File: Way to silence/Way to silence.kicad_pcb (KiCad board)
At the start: 2 copper layers, 60 parts, among them J1 SD Card Connector, J2 Screw_Terminal_01x02, J3 5V_Terminal, J4 Battery_Terminal, Q1 BC817, Q2 BC817, SW1 SW_SPDT, U1 ESP32-WROOM-32-N16, U2 SM5308, U3 CP2102-GMR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

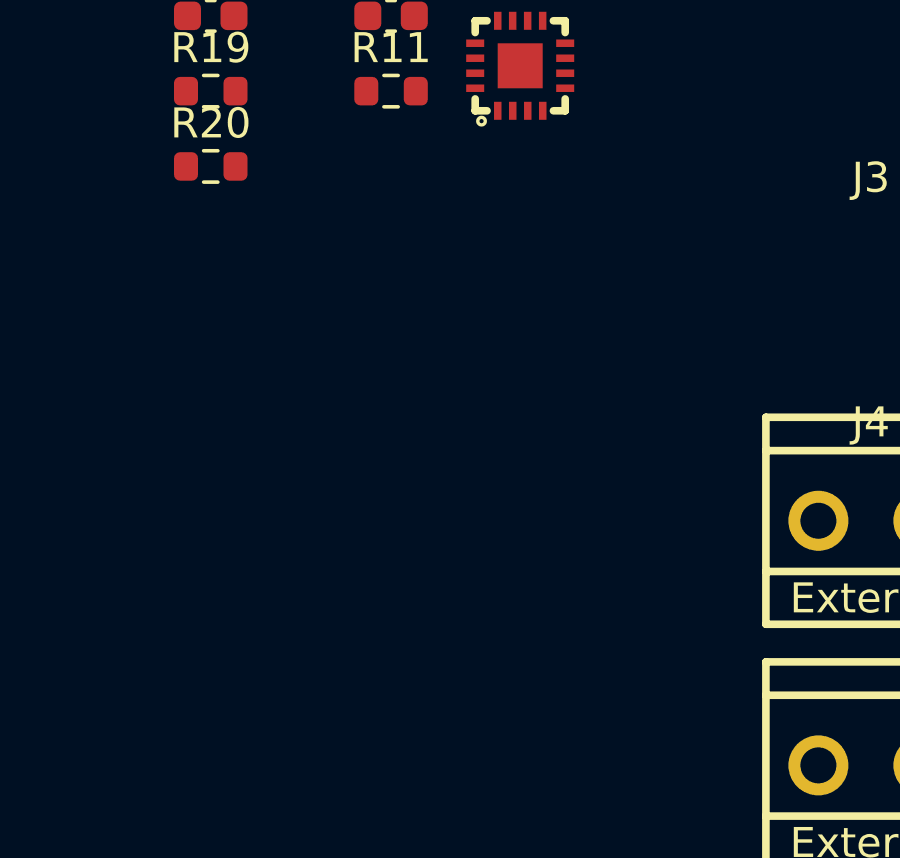
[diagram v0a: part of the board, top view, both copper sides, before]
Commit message: [ADD] Missing footprints
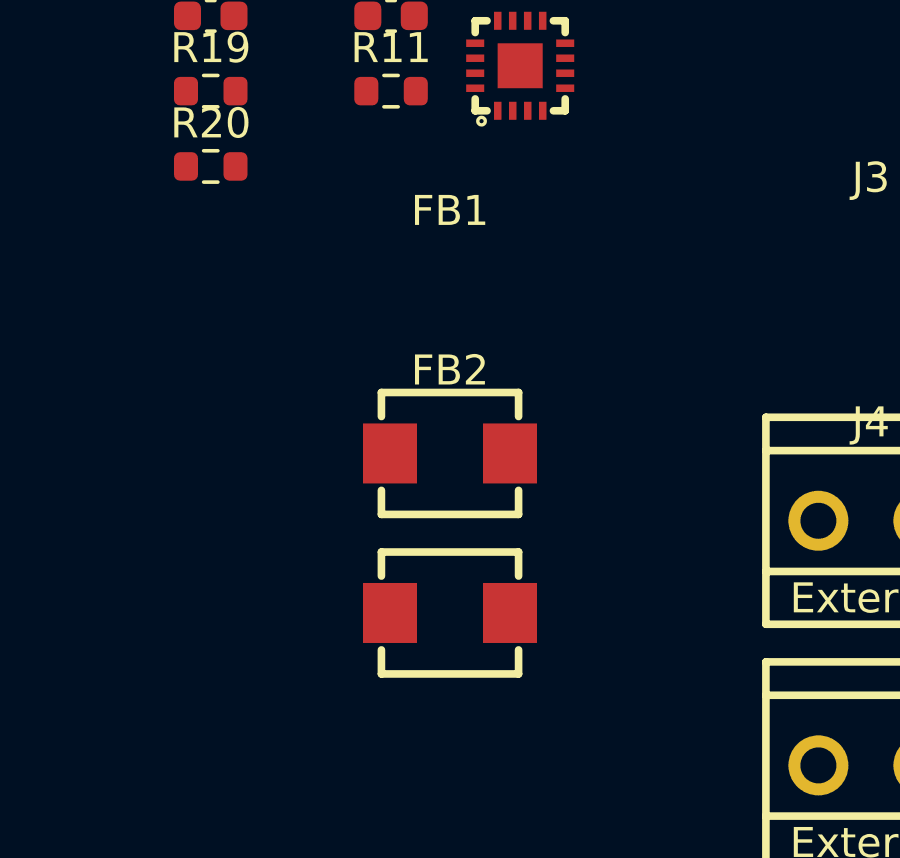
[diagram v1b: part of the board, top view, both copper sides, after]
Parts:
- added FB1: FerriteBead, Way to silence:Inductor, F.Cu at (111.2, 55.6)
- added FB2: FerriteBead, Way to silence:Inductor, F.Cu at (111.2, 61.0)
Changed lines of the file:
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@@
     )
   )
+  (footprint "Way to silence:Inductor" (layer "F.Cu")
+    (at 111.22 55.642)
+    (property "LCSC" "C2847468")
+    (property "Sheetfile" "I2SAmp.kicad_sch")
+    (property "Sheetname" "I2S Amp")
+    (property "ki_description" "Ferrite bead")
+    (property "ki_keywords" "L ferrite bead inductor filter")
+    (attr smd)
+    (fp_text reference "FB1" (at 0 -8.08 unlocked) (layer "F.SilkS")
+        (effects (font (size 1 1) (thickness 0.1)))
+    )
+    (fp_text value "FerriteBead" (at 0 -6.58 unlocked) (layer "F.Fab")
+        (effects (font (size 1 1) (thickness 0.15)))
+    )
+    (fp_text user "${REFERENCE}" (at 0 -5.08 unlocked) (layer "F.Fab")
+        (effects (font (size 1 1) (thickness 0.15)))
+    )
+    (fp_line (start -2.286 -2.032) (end 2.286 -2.032)
+      (stroke (width 0.254) (type solid)) (layer "F.SilkS"))
+    (fp_line (start -2.286 -1.231) (end -2.286 -2.032)
+      (stroke (width 0.254) (type solid)) (layer "F.SilkS"))
+    (fp_line (start -2.286 2.032) (end -2.286 1.231)
+      (stroke (width 0.254) (type solid)) (layer "F.SilkS"))
+    (fp_line (start 2.286 -2.032) (end 2.286 -1.231)
+      (stroke (width 0.254) (type solid)) (layer "F.SilkS"))
+    (fp_line (start 2.286 1.231) (end 2.286 2.032)
+      (stroke (width 0.254) (type solid)) (layer "F.SilkS"))
+    (fp_line (start 2.286 2.032) (end -2.286 2.032)
+      (stroke (width 0.254) (type solid)) (layer "F.SilkS"))
+    (pad "1" smd rect (at -2 0 90) (size 2 1.8) (layers "F.Cu" "F.Paste" "F.Mask")
+      (net 93 "Net-(U4-OUTN)") (pintype "passive"))
+    (pad "2" smd rect (at 2 0 90) (size 2 1.8) (layers "F.Cu" "F.Paste" "F.Mask")
+      (net 5 "Net-(J2-Pin_2)") (pintype "passive"))
+  )
   (footprint "Way to silence:R_0603_1608Metric" (layer "F.Cu")
     (at 81.965 98.425)
@@
       (net 16 "Net-(D3-A)") (pinfunction "A") (pintype "passive"))
   )
+  (footprint "Way to silence:Inductor" (layer "F.Cu")
+    (at 111.22 60.96)
+    (property "LCSC" "C2847468")
+    (property "Sheetfile" "I2SAmp.kicad_sch")
+    (property "Sheetname" "I2S Amp")
+    (property "ki_description" "Ferrite bead")
+    (property "ki_keywords" "L ferrite bead inductor filter")
+    (attr smd)
+    (fp_text reference "FB2" (at 0 -8.08 unlocked) (layer "F.SilkS")
+        (effects (font (size 1 1) (thickness 0.1)))
+    )
+    (fp_text value "FerriteBead" (at 0 -6.58 unlocked) (layer "F.Fab")
+        (effects (font (size 1 1) (thickness 0.15)))
+    )
+    (fp_text user "${REFERENCE}" (at 0 -5.08 unlocked) (layer "F.Fab")
+        (effects (font (size 1 1) (thickness 0.15)))
+    )
+    (fp_line (start -2.286 -2.032) (end 2.286 -2.032)
+      (stroke (width 0.254) (type solid)) (layer "F.SilkS"))
+    (fp_line (start -2.286 -1.231) (end -2.286 -2.032)
+      (stroke (width 0.254) (type solid)) (layer "F.SilkS"))
+    (fp_line (start -2.286 2.032) (end -2.286 1.231)
+      (stroke (width 0.254) (type solid)) (layer "F.SilkS"))
+    (fp_line (start 2.286 -2.032) (end 2.286 -1.231)
+      (stroke (width 0.254) (type solid)) (layer "F.SilkS"))
+    (fp_line (start 2.286 1.231) (end 2.286 2.032)
+      (stroke (width 0.254) (type solid)) (layer "F.SilkS"))
+    (fp_line (start 2.286 2.032) (end -2.286 2.032)
+      (stroke (width 0.254) (type solid)) (layer "F.SilkS"))
+    (pad "1" smd rect (at -2 0 90) (size 2 1.8) (layers "F.Cu" "F.Paste" "F.Mask")
+      (net 92 "Net-(U4-OUTP)") (pintype "passive"))
+    (pad "2" smd rect (at 2 0 90) (size 2 1.8) (layers "F.Cu" "F.Paste" "F.Mask")
+      (net 6 "Net-(J2-Pin_1)") (pintype "passive"))
+  )
   (footprint "Way to silence:LED_0603" (layer "F.Cu")

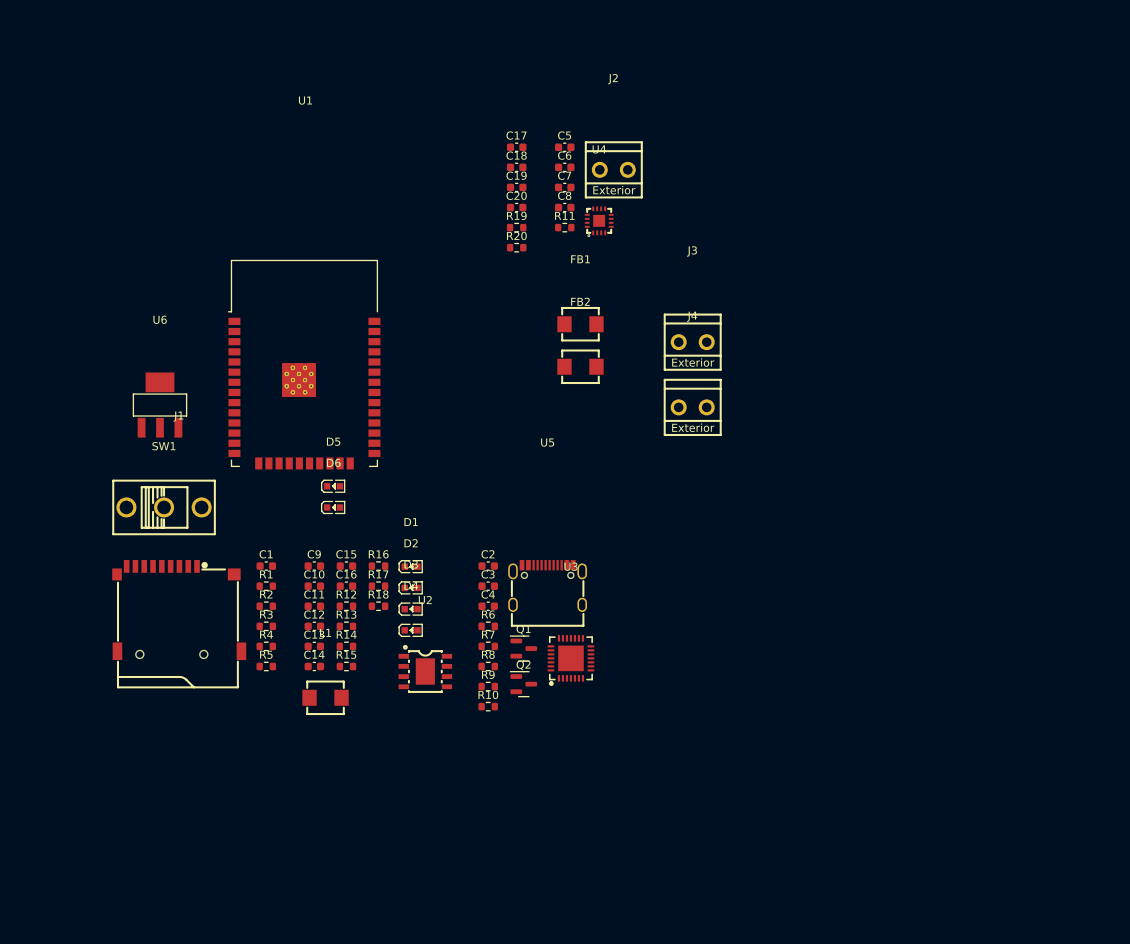
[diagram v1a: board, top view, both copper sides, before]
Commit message: [ADD] Beg of routing
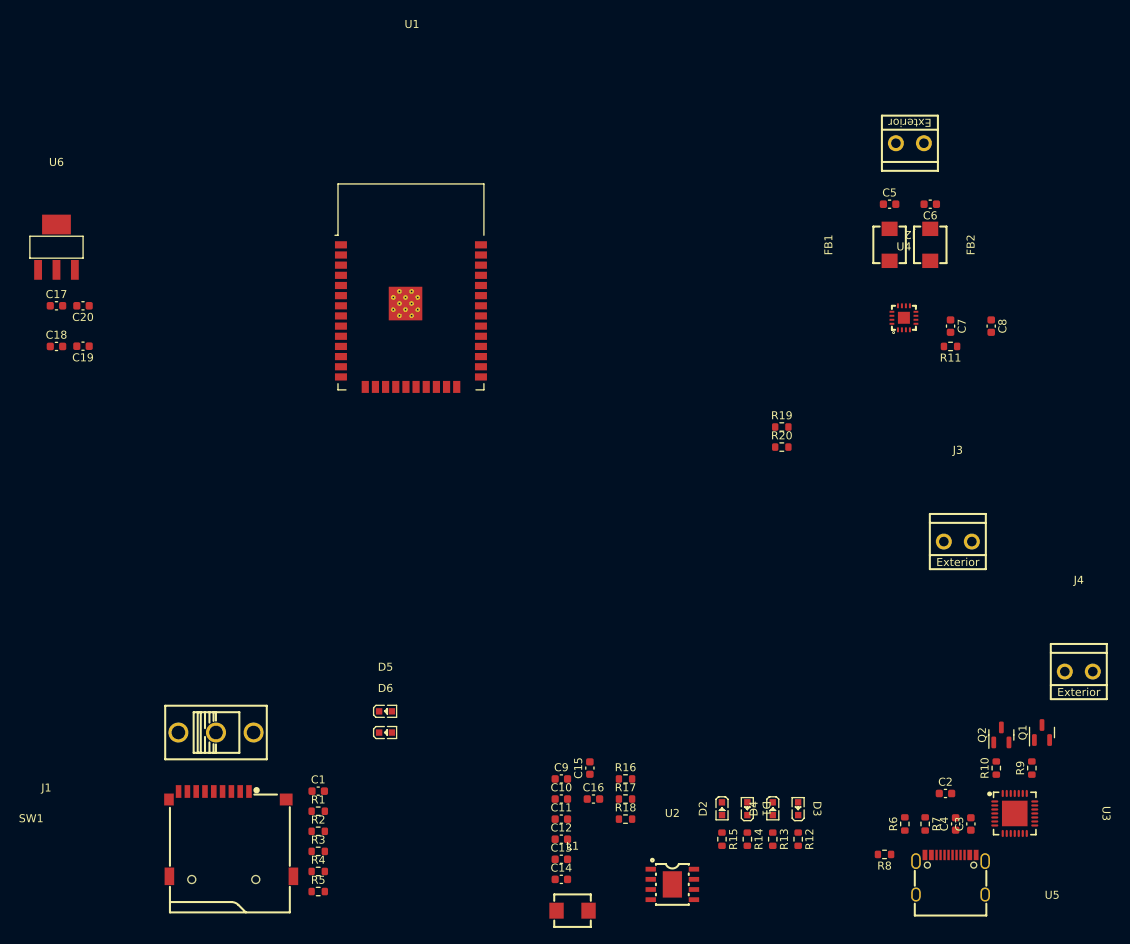
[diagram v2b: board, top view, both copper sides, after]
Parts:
- J2: value Screw_Terminal_01x02 -> Amplificator_Terminal
- moved R9 68.7 mm to (167.6, 111.1), turned to 90 degrees
- moved C3 67.3 mm to (160.0, 118.1), turned to 90 degrees
- moved Q1 65.6 mm to (168.9, 106.7), turned to 90 degrees
- moved C4 64.5 mm to (158.1, 118.1), turned to 90 degrees
- moved R10 64.0 mm to (163.2, 111.1), turned to 90 degrees
- moved C2 63.8 mm to (156.8, 114.3)
- moved R12 63.5 mm to (138.4, 120.0), turned to -90 degrees
- moved U5 62.0 mm to (157.5, 124.5)
- moved C18 61.7 mm to (45.7, 58.4)
- moved C17 60.8 mm to (45.7, 53.3)
- moved Q2 60.0 mm to (163.8, 107.0), turned to 90 degrees
- moved R13 59.6 mm to (135.3, 120.0), turned to -90 degrees
- moved R7 59.0 mm to (154.3, 118.1), turned to -90 degrees
- moved U3 58.8 mm to (165.5, 116.8), turned to -90 degrees
- moved J4 58.5 mm to (173.5, 99.1)
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
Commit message: [ADD] i2S Module placed
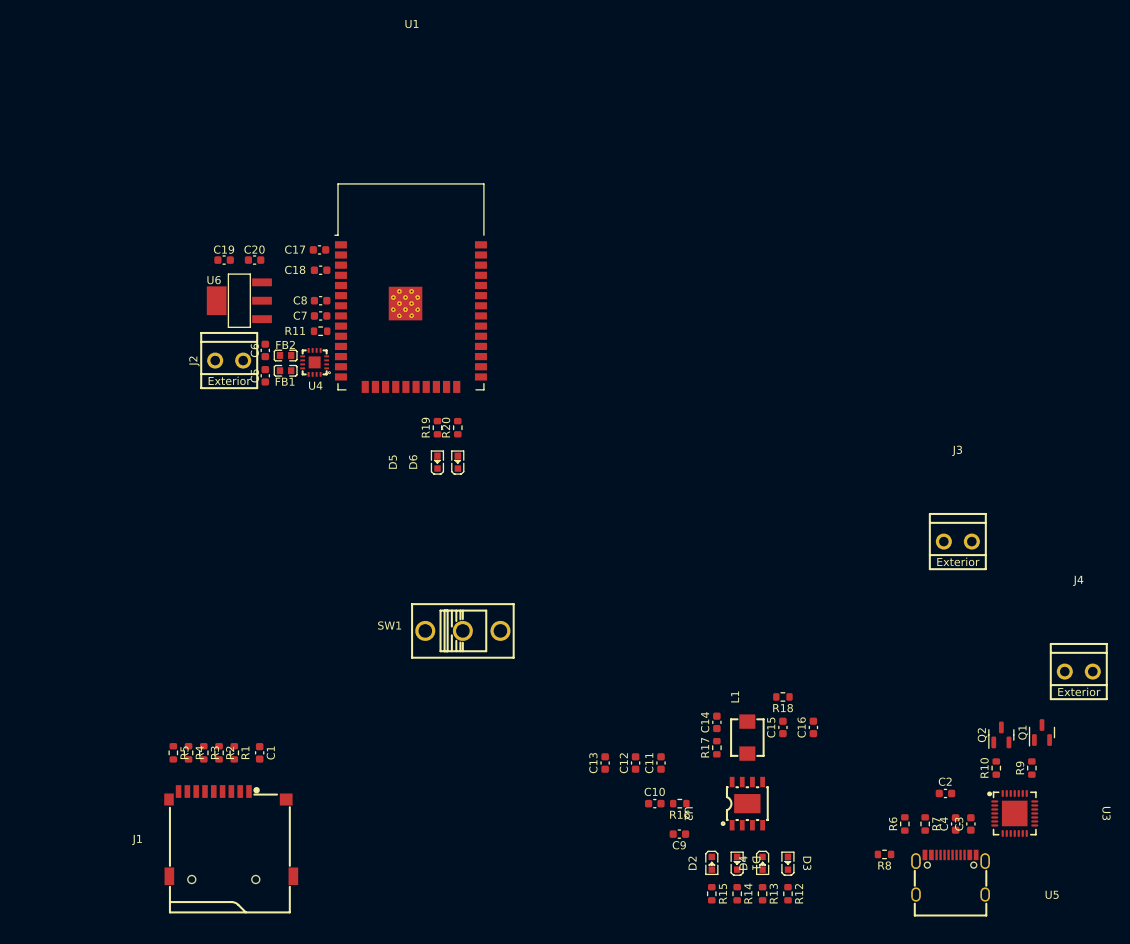
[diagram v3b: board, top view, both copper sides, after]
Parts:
- FB1, FB2: footprint Way to silence:Inductor -> Way to silence:FB_0603
- moved J2 89.3 mm to (67.3, 60.2), turned to 0 degrees
- moved C6 85.1 mm to (71.8, 58.9), turned to -90 degrees
- moved C8 83.9 mm to (78.7, 52.7), turned to 0 degrees
- moved FB2 81.8 mm to (74.4, 59.5), turned to 180 degrees
- moved C5 80.9 mm to (71.8, 62.1), turned to 90 degrees
- moved R11 78.8 mm to (78.7, 56.5), turned to 0 degrees
- moved C7 78.8 mm to (78.7, 54.6), turned to 0 degrees
- moved FB1 77.1 mm to (74.4, 61.5), turned to 180 degrees
- moved U4 73.9 mm to (78.0, 60.4), turned to 90 degrees
- moved R19 43.0 mm to (93.3, 68.6), turned to 90 degrees
- moved R20 40.6 mm to (95.9, 68.6), turned to 90 degrees
- moved D6 35.0 mm to (95.9, 72.9), turned to 90 degrees
- moved C18 34.4 mm to (78.7, 48.9)
- moved C17 33.6 mm to (78.6, 46.4)
- moved SW1 33.4 mm to (96.5, 94.0)
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
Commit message: [ADD] Routing placement seems ok
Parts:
- moved U5 101.4 mm to (68.6, 75.8)
- moved C2 100.2 mm to (69.4, 65.4)
- moved C3 99.5 mm to (73.0, 69.8)
- moved C4 99.5 mm to (71.1, 69.8)
- moved R7 98.4 mm to (68.6, 69.8)
- moved R6 97.8 mm to (66.7, 69.8)
- moved R9 96.6 mm to (80.0, 70.5)
- moved U3 96.6 mm to (78.1, 75.8)
- moved Q1 96.5 mm to (81.0, 67.0)
- moved R10 96.0 mm to (76.2, 70.5)
- moved Q2 95.3 mm to (77.3, 67.0)
- moved R8 84.7 mm to (75.6, 80.0), turned to 0 degrees
- moved J1 79.4 mm to (111.7, 53.3), turned to 90 degrees
- moved J3 71.7 mm to (86.8, 78.7)
- moved C1 67.8 mm to (103.3, 49.5), turned to 0 degrees
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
